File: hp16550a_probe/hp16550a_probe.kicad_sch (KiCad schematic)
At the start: 5 parts

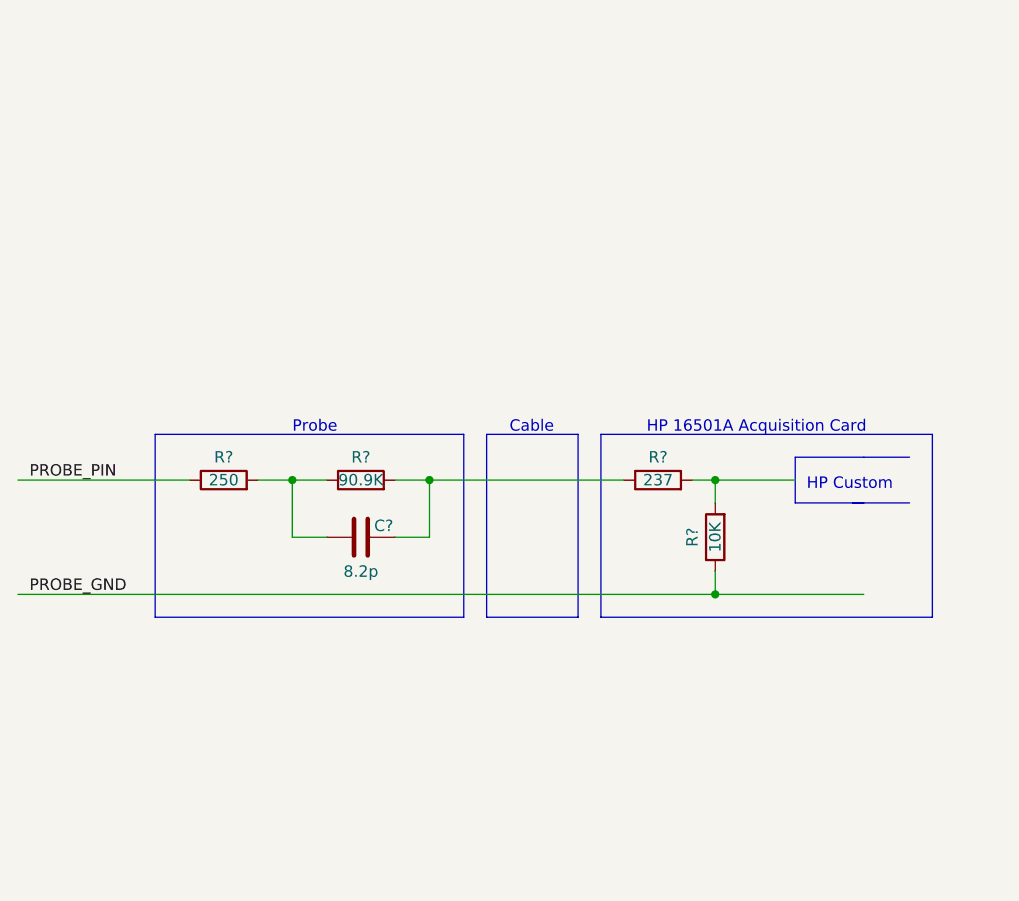
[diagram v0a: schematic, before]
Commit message: Add schematic of a few logic analyzers.
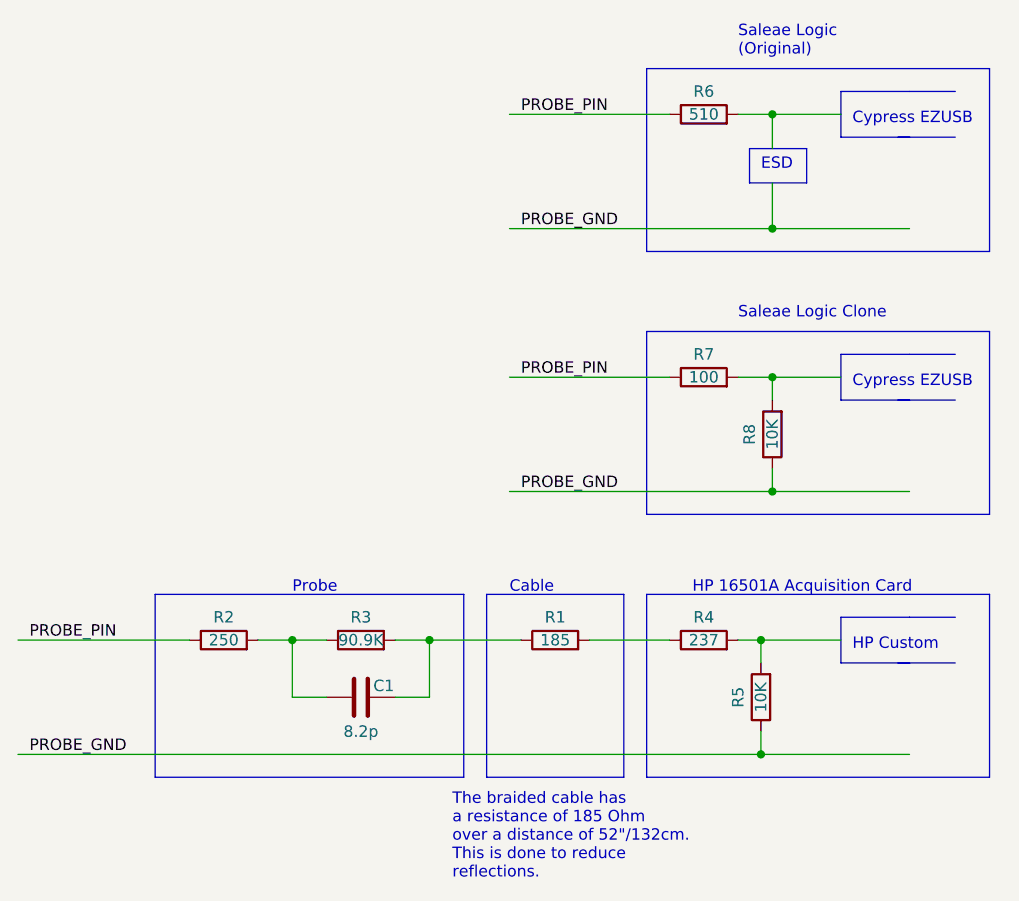
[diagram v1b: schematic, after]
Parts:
- added R1: 185, symbol Device:R
- added R6: 510, symbol Device:R
- added R7: 100, symbol Device:R
- added R8: 10K, symbol Device:R
- gave numbers to parts that had none: 5
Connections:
- net PROBE_GND: now also R8.1
- net PROBE_PIN: now also R6.1, R7.1
- net at C1.2, R3.2: now also R1.1; no longer R4.1
- new net: R7.2, R8.2
- new net: R1.2, R4.1
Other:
- note added: "Cypress EZUSB"
- note added: "ESD"
- note added: "Saleae Logic (Original)"
- note added: "Saleae Logic Clone"
- note added: "The braided cable has a resistance of 185 Ohm over a distance of 52"/132cm. This is done to reduce reflections."
- moved on the sheet: C1, R2, R3, R4, R5

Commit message: hp16550a. Unknown changes.
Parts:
- added R10, R11, R15, R17: 100k, symbol Device:R
- added R12, R16: 33, symbol Device:R
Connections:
- net PROBE_PIN: now also R10.1, R15.1
- net PROBE_GND renamed GND
- net GND: now also R11.1, R17.1
- new net: R10.2, R11.2, R12.1
- new net: R15.2, R16.1, R17.2
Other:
- added sheet theoretical_probes (untitled.kicad_sch)
- note added: "+"
- note added: "-"
- note added: "DSLogic U3Pro16"
- note added: "LVDS"
- note added: "Probe Wire"
- note added: "SVR05-4"
- note added: "Spartan-6 FPGA"
- note added: "The braided cable has a resistance of 185 Ohm over a distance of 52"/132cm. This is done to reduce reflections. C and L unknown."
- note removed: "The braided cable has a resistance of 185 Ohm over a distance of 52"/132cm. This is done to reduce reflections."
- moved on the sheet: C1, R1, R2, R3, R4, R5, R6, R7, R8
